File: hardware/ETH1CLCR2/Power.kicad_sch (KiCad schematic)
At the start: 38 parts, among them Q901 IRFR5410, U901 LM1117SX-3.3/NOPB, U902 NCS3S1205SC, U903 MAX5902, U904 LM1117SX-5.0/NOPB, U905 NMK2409SAC, U906 LM1117SX-5.0/NOPB, U907 NMK2409SC, U908 LM2990SX-5.0

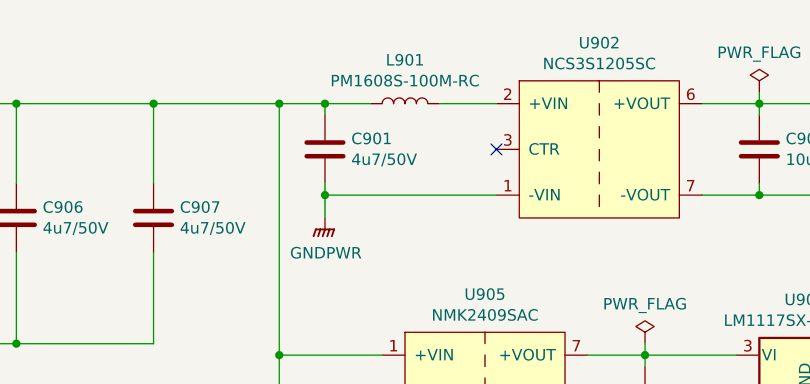
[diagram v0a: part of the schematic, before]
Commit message: Converted HW files to KiCAD 7.0.
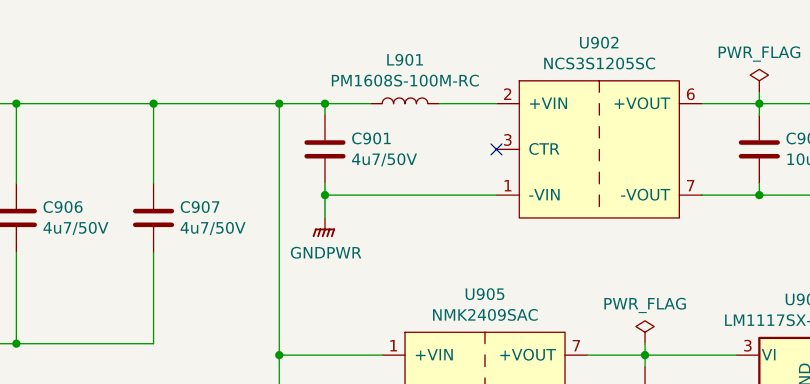
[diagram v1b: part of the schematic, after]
